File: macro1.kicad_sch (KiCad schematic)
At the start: 30 parts, among them J1 AVR-ISP-6, SW1 Macro1, SW2 Macro2, SW3 Macro3, SW4 Macro4, SW5 PUSH_RESET, U1 ATmega32U4-A, U2 PRTR5V0U2X, Y1 XTAL

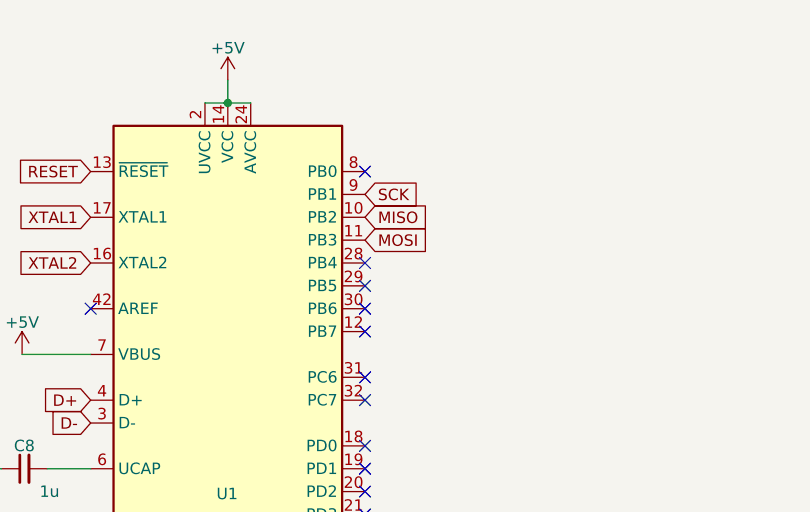
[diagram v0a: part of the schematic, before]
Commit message: MOSI Fix
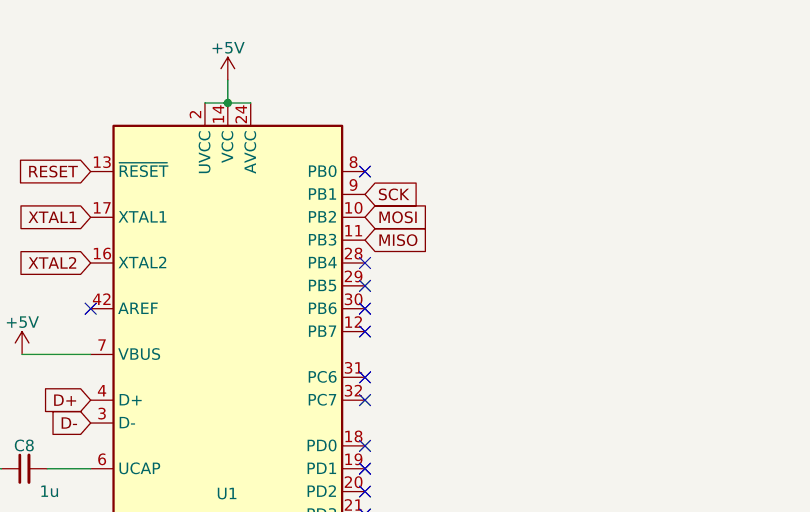
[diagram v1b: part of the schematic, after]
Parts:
- FB1: footprint (none) -> Inductor_SMD:L_0805_2012Metric_Pad1.15x1.40mm_HandSolder
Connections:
- net MISO: now also U1.11 (PB3); no longer U1.10 (PB2)
- net MOSI: now also U1.10 (PB2); no longer U1.11 (PB3)
